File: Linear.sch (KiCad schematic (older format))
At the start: 61 parts, among them Q10 D45H11, Q11 MMBT3904, Q12 PZT3904, Q8 4403, Q9 2N7002PW, U1 OPA2376AID, U2 LM358M, U3 LM393M, U4 LM393M

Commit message: Finish PCB
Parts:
- removed C17, C18, C25, C27, C29, C30: 22n, IPC7351-Nominal:CAPC1608X55, symbol C-0603
- removed C19, C20, C21, C23: 100n, IPC7351-Nominal:CAPC1608X55, symbol C-0603
- removed C28: 220p, IPC7351-Nominal:CAPC1608X55, symbol C-0603
- removed Q11: MMBT3904, smd-semi:SOT-23, symbol MMBT3904
- removed R13, R14, R17, R18, R19, R20, R26, R27, R31, R33, R36: 2k, IPC7351-Nominal:RESC1608X50, symbol R-0603
- removed R15, R16, R21, R23, R24, R25, R29, R30: 22k, IPC7351-Nominal:RESC1608X50, symbol R-0603
- removed R22, R32, R37: 348, IPC7351-Nominal:RESC1608X50, symbol R-0603
- removed R34, R35, R38: 470k, IPC7351-Nominal:RESC1608X50, symbol R-0603
- removed U1: OPA2376AID, IPC7351-Nominal:SOIC127P600X175-8, symbol OPA2376AID
- removed U2: LM358M, IPC7351-Nominal:SOIC127P600X175-8, symbol LM358M
- added C17, C18, C25, C27, C29, C30: 22n, IPC7351-Nominal:CAPC1005X55, symbol C-0402
- added C19, C20, C21, C23: 100n, IPC7351-Nominal:CAPC1005X55, symbol C-0402
- added C28: 220p, IPC7351-Nominal:CAPC1005X55, symbol C-0402
- added Q11: PMSS3904, smd-semi:SC-70, symbol PMSS3904
- added R13, R14, R17, R18, R19, R20, R26, R27, R31, R33, R36: 2k, IPC7351-Nominal:RESC1005X40, symbol R-0402
- added R15, R16, R21, R23, R24, R25, R29, R30: 22k, IPC7351-Nominal:RESC1005X40, symbol R-0402
- added R22, R32, R37: 348, IPC7351-Nominal:RESC1005X40, symbol R-0402
- added R34, R35, R38: 470k, IPC7351-Nominal:RESC1005X40, symbol R-0402
- added U1: OPA2376AIDGK, IPC7351-Nominal:SOP65P490X110-8, symbol OPA2376AIDGK
- added U2: LM358DGK, IPC7351-Nominal:SOP65P490X110-8, symbol LM358DGK
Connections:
- net +3.3: now also R34.2, R35.2, R36.2, R38.2
- net GND: now also C19.2, C20.2, C21.2, C23.2, C29.1, C30.1, R37.1
- net ISENSE: now also R18.2
- net ISENSE_OUT: now also R21.2, R27.2, U1.1 (OUT)
- net ISET: now also U2.3 (IN+)
- net OVP_THRESH: now also R17.2
- net P_IN: now also Q11.3, R23.2, R30.2, R31.2
- net REFGND: now also R20.1, R22.1
- net V+: now also R29.2, U2.8 (V+)
- net V-: now also C21.1, C23.1, U1.4 (V-), U2.4 (V-)
- net VSENSE+: now also R14.2, R16.2
- net VSENSE-: now also R13.2, R15.2
- net VSENSE_OUT: now also C25.2, R19.1, R25.2, U1.7 (OUT)
- net VSET: now also U2.5 (IN+)
- net ~EN: now also R29.1
- net ~ILIM: now also C30.2, R35.1
- net ~SCR_TRIPPED: now also R38.1
- net ~VLIM: now also C29.2, R34.1
- net at Q10.1, Q12.2, Q12.4: now also R31.1
- net at D3.2, TP11.1, U3.3 (IN+): now also C28.1, U2.7 (OUT)
- net at D3.1, TP12.1, U3.5 (IN+): now also C27.1, U2.1 (OUT)
- net at D3.3, Q9.3, TP13.1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: now also R32.1
- net at D4.1, Q12.1: now also Q11.2, R33.2
- net at D4.3, E1.2, Q12.3: now also R33.1
- net at D4.2: now also Q11.1, R30.1, R32.2
- net at Q8.1: now also R23.1, R24.2
- net at U4.1 (OUT): now also R24.1
- net at U4.3 (IN+): now also C19.1, R17.1
- net at U4.5 (IN+): now also R36.1, R37.2
- new net: C18.1, R16.1, R20.2, U1.5 (IN+)
- new net: C17.1, R15.1, R19.2, U1.6 (IN-)
- new net: R21.1, R22.2, U1.2 (IN-)
- new net: R18.1, U1.3 (IN+)
- new net: C28.2, R25.1, R26.1, U2.6 (IN-)
- new net: C27.2, R27.1, U2.2 (IN-)
- new net: C25.1, R26.2
- new net: C17.2, R13.1
- new net: C18.2, R14.1
- new net +3.3A: C20.1, U1.8 (V+)

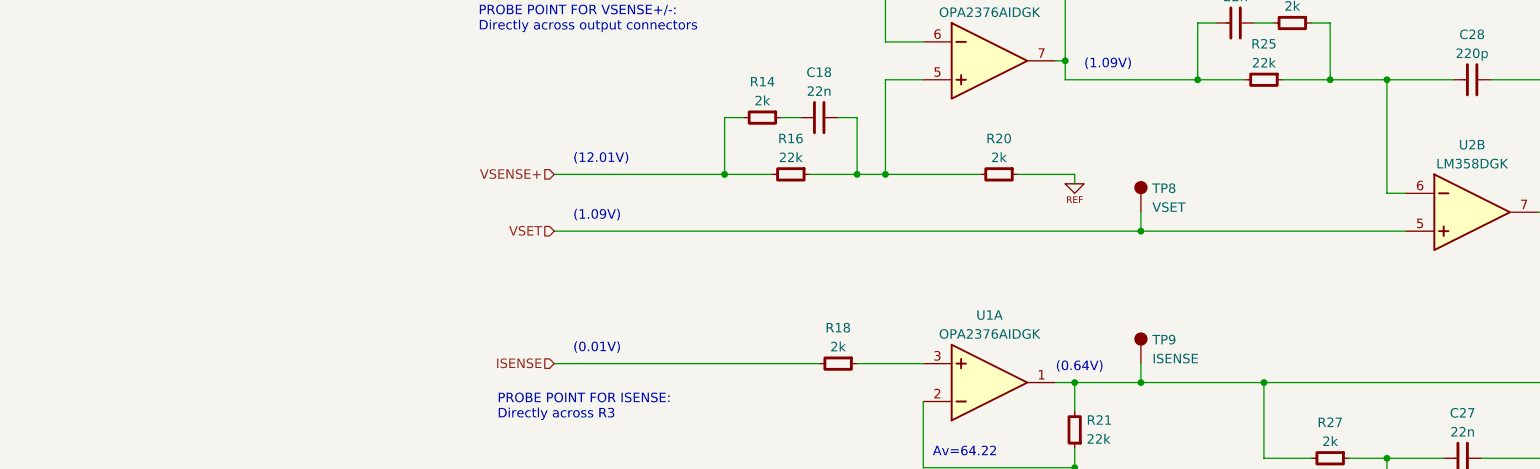
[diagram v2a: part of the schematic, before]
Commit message: Fix output blip
Add a bodge wire to prototype to allow the MCU to force the regulator
into saturation-low
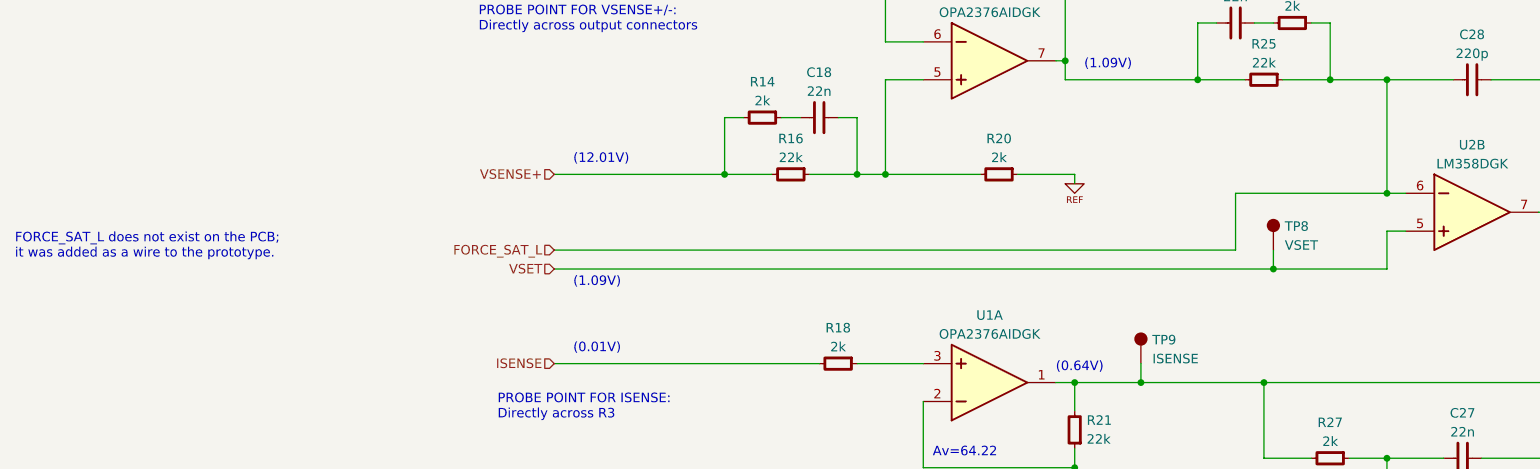
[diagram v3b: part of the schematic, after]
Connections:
- net FORCE_SAT_L: now reaches C28.2, R25.1, R26.1, U2.6 (IN-)
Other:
- note added: "FORCE_SAT_L does not exist on the PCB;\nit was added as a wire to the prototype."
- moved on the sheet: TP8
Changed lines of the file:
@@
 Text Notes 6850 850  0    50   ~ 0
 On heatsink
-Text HLabel 1100 4500 0    50   Input ~ 0
+Text HLabel 1100 4700 0    50   Input ~ 0
 VSET
 Text HLabel 1100 6200 0    50   Input ~ 0
@@
 	1100 6200 5600 6200
 Wire Wire Line
-	1100 4500 5600 4500
+	1100 4700 5500 4700
 Wire Wire Line
 	5500 6000 5600 6000
@@
 	6000 5700 6400 5700
 Wire Wire Line
-	5500 4300 5600 4300
+	4700 4300 5600 4300
 Wire Wire Line
 	5500 3700 5500 4300
@@
 Text Notes 1200 4150 0    50   ~ 0
 (12.01V)
-Text Notes 1200 4450 0    50   ~ 0
+Text Notes 1200 4800 0    50   ~ 0
 (1.09V)
 Text Notes 1200 5150 0    50   ~ 0
@@
 L TESTPOINT TP8
 U 1 1 55E06BC9
-P 4200 4400
-F 0 "TP8" H 4260 4525 50  0000 L CNN
-F 1 "VSET" H 4260 4425 50  0000 L CNN
-F 2 "conn-test:TEST-SMD-SMALL" H 4260 4375 50  0001 L CNN
-F 3 "" H 4200 4400 50  0000 C CNN
-	1    4200 4400
-	1    0    0    -1
-$EndComp
-Wire Wire Line
-	4200 4400 4200 4500
-Connection ~ 4200 4500
+P 4900 4600
+F 0 "TP8" H 4960 4725 50  0000 L CNN
+F 1 "VSET" H 4960 4625 50  0000 L CNN
+F 2 "conn-test:TEST-SMD-SMALL" H 4960 4575 50  0001 L CNN
+F 3 "" H 4900 4600 50  0000 C CNN
+	1    4900 4600
+	1    0    0    -1
+$EndComp
+Wire Wire Line
+	4900 4600 4900 4700
+Connection ~ 4900 4700
 $Comp
 L TESTPOINT TP9
@@
 	-1   0    0    1
 $EndComp
+Wire Wire Line
+	5500 4700 5500 4500
+Wire Wire Line
+	5500 4500 5600 4500
+Text HLabel 1100 4600 0    50   Input ~ 0
+FORCE_SAT_L
+Wire Wire Line
+	1100 4600 4700 4600
+Wire Wire Line
+	4700 4600 4700 4300
+Connection ~ 5500 4300
+Text Notes -1750 4650 0    50   ~ 0
+FORCE_SAT_L does not exist on the PCB;\nit was added as a wire to the prototype.
 $EndSCHEMATC

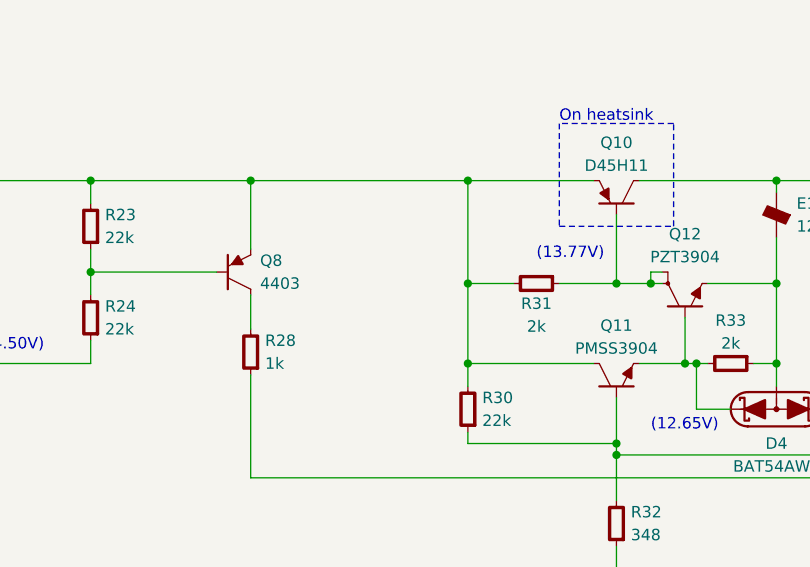
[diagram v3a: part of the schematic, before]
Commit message: Add PSRR improvement
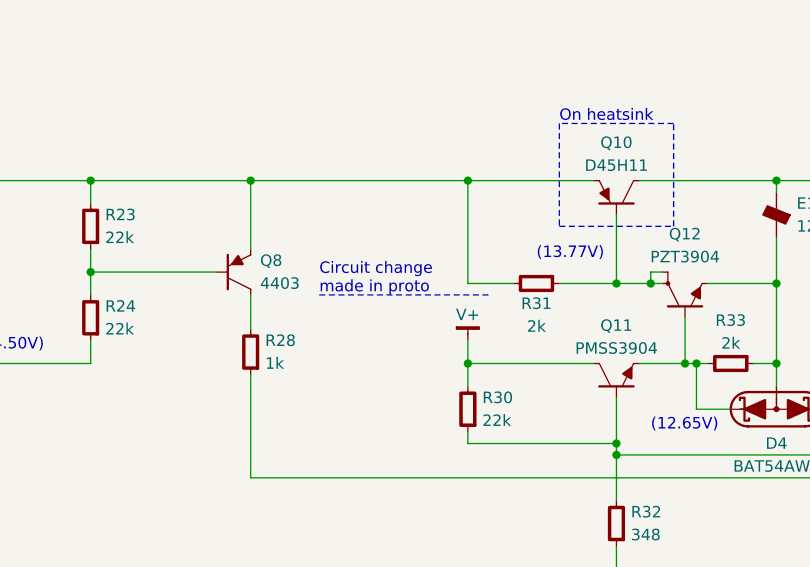
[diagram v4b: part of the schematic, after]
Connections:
- net P_IN: no longer Q11.3, R30.2
- net V+: now also Q11.3, R30.2
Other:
- note added: "Circuit change\nmade in proto"
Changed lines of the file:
@@
 Wire Notes Line
 	6850 850  6850 1300
-Connection ~ 6450 1550
 Wire Wire Line
 	6450 1900 7000 1900
 Wire Wire Line
 	6450 1550 6650 1550
-Wire Wire Line
-	6450 1100 6450 2000
 Wire Wire Line
 	1100 1100 7000 1100
@@
 Text Notes -1750 4650 0    50   ~ 0
 FORCE_SAT_L does not exist on the PCB;\nit was added as a wire to the prototype.
+Wire Wire Line
+	6450 1800 6450 2000
+Wire Wire Line
+	6450 1550 6450 1100
+$Comp
+L V+ #PWR?
+U 1 1 56438D50
+P 6450 1800
+F 0 "#PWR?" H 6450 1850 30  0001 C CNN
+F 1 "V+" H 6450 1913 50  0000 C CNN
+F 2 "" H 6450 1800 60  0000 C CNN
+F 3 "" H 6450 1800 60  0000 C CNN
+	1    6450 1800
+	1    0    0    -1
+$EndComp
+Wire Notes Line
+	5800 1600 6550 1600
+Text Notes 5800 1600 0    50   ~ 0
+Circuit change\nmade in proto
 $EndSCHEMATC
